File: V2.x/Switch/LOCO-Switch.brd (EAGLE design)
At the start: 43.2 x 34.3 mm, 55 parts, among them IC1 Atmega 328-P, IC2 MCP2515, IC3 ACS712ELCTR-20A-T, IC5 LM340MP-05, J1 3-794618-4, J2 3-794618-4, Q1 8MHz, Q2 16MHz, Q3 FDS5680, Q4 FDS5680, Q5 FDS5680, Q6 FDS5680, Q7 FDS5680, Q8 FDS5680, X1 22-23-2081

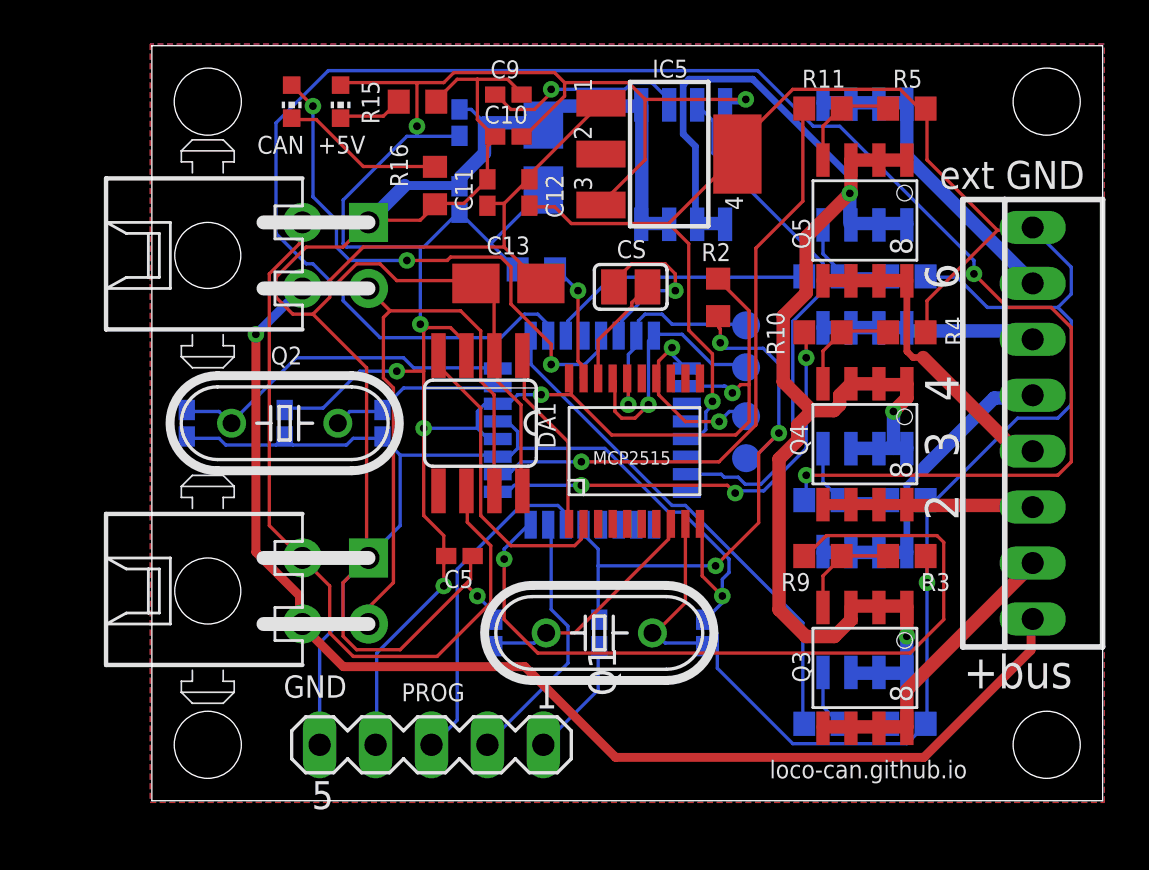
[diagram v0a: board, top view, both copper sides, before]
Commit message: update switch board
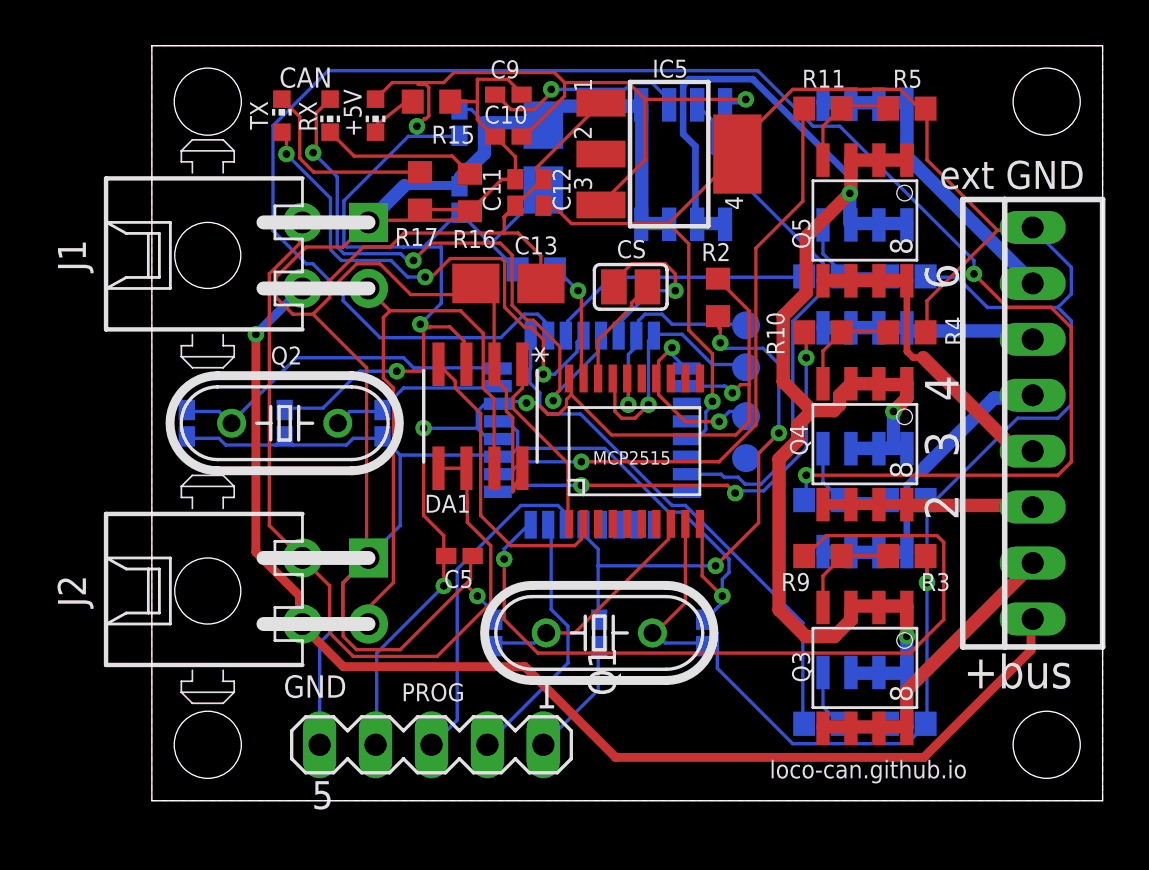
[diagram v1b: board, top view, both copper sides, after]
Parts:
- removed CAN: GRN, led:CHIP-LED0603
- added R17: 33R, rcl:R0603
- added RX: RD, led:CHIP-LED0603
- added TX: WRT, led:CHIP-LED0603
- DA1: value TJA1050 -> MCP2551-X/SNSOIC8-N_MC_MCH; device TJA1050:SO08 -> MCP2551:SOIC8-N_MC_MCH
- IC2: device mcp2514:TSSOP20 -> MCP2515:TSSOP20
- J1, J2: device SamacSys_Parts:SHDRRA4W102P300_2X2_686X892X73 -> Micro Mate-N-Lok:3-794618-4
- PROG: device con-lstb:MA05-1 -> lst-b:MA05-1
- R16: value 10k -> 33R
- moved +5V 1.71 mm to (10.2, 31.1)
- moved R16 1.62 mm to (14.4, 27.6)
- moved C11 1.27 mm to (16.5, 27.6)
- moved C12 0.64 mm to (17.8, 27.6)
- moved R15 0.63 mm to (12.7, 31.8)
- moved DA1 0.32 mm to (14.9, 17.5), turned to 270 degrees
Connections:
- new net N$13: R17.1, TX.C
- new net N$14: IC1.12, TX.A
- net CAN-L: now also DA1.5
- net D9: now also RX.A; no longer CAN.A
- net GND: now also R17.2
- net N$9: now also RX.C; no longer CAN.C
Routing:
- net N$14: track 0.00 -> 23.9 mm, vias 0 -> 3
- net N$13: track 0.00 -> 8.74 mm
- net GND: track 242.2 -> 245.8 mm
- net D9: track 25.0 -> 27.9 mm
- net CAN-L: track 34.8 -> 37.0 mm
- net VCC: track 116.6 -> 118.2 mm
- net D5: track 23.2 -> 24.1 mm
- net CAN-H: track 28.4 -> 29.3 mm
- net +12V: track 77.8 -> 78.4 mm
- net N$12: track 2.94 -> 2.33 mm
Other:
- board text added: "CAN"
